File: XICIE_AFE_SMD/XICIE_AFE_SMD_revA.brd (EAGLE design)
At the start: 100 x 80 mm, 14 parts, among them IC1 LM324D, Q1 MOSFET-NCHANNELBSS123LT1G, Q2 MOSFET-NCHANNELBSS123LT1G

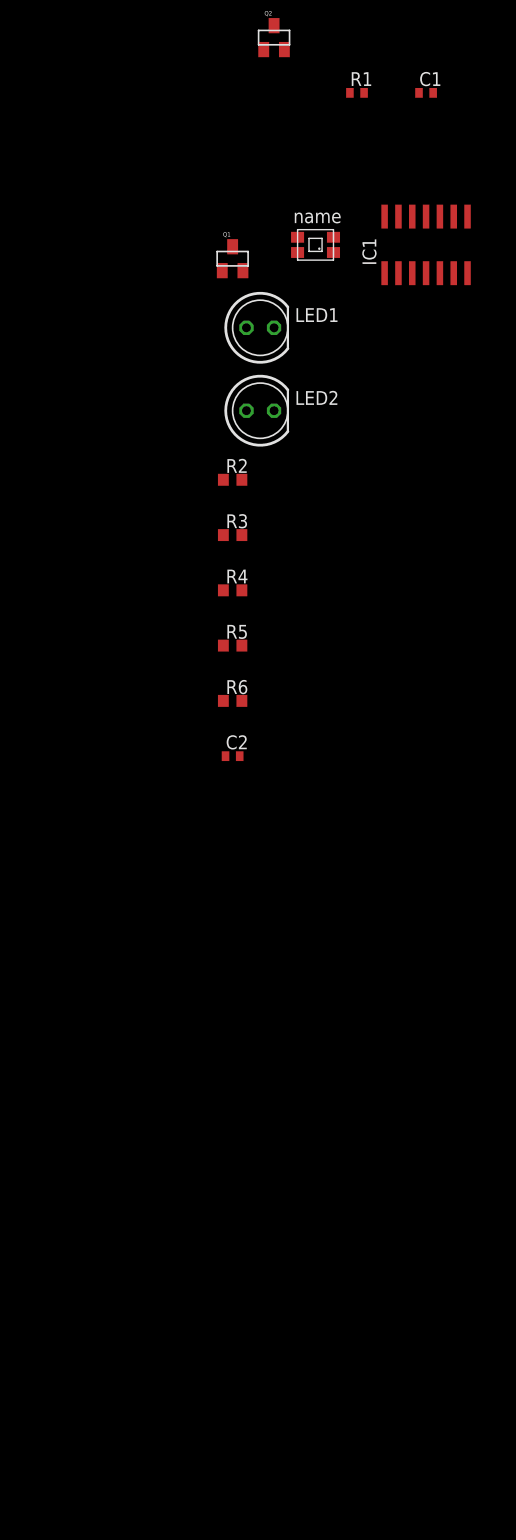
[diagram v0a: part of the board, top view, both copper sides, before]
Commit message: Added PSoc IC and boost converter
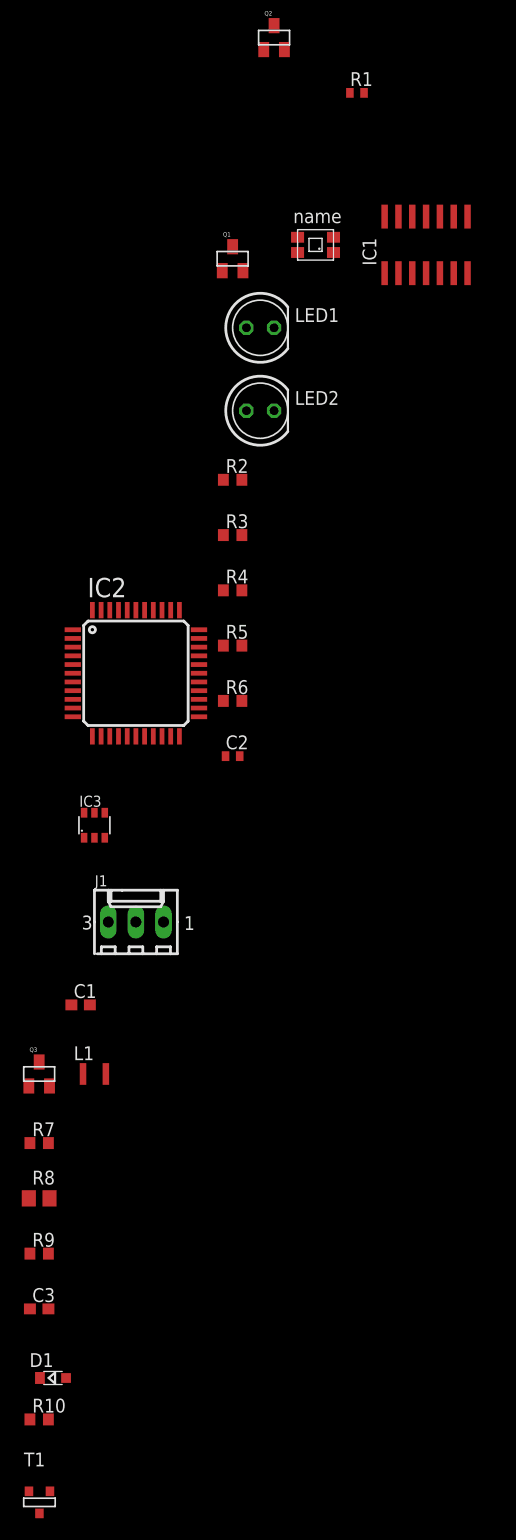
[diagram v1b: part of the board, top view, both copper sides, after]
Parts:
- added C3: 4.7 uF, rcl:C0603
- added D1: (no value), juliano:SMINI2-F5-B
- added IC2: CY8C4245T, juliano:TQFP44
- added IC3: AAT1217, juliano:SOT23-6
- added J1: 22-27-2031-03, con-molex:6410-03
- added L1: 4.7 uH, juliano:L2518
- added Q3: MOSFET-NCHANNELBSS123LT1G, SparkFun-DiscreteSemi:SOT23
- added R10, R7: 510 K, rcl:R0603
- added R8: 1.02 M, rcl:R0805
- added R9: 604 K, rcl:R0603
- added T1: (no value), zetex:SOT-23
- C1: value 270 pF -> 4.7 uF; device rcl:C0402 -> rcl:C0603
- moved C1 89.6 mm to (-50.8, -66.0)
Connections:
- removed net IN_VREF: R6.2
- removed net TRANSOUT: C1.2, IC1.1, R1.2
- new net N$10: C1.1, IC3.6, J1.3, L1.1
- new net N$11: D1.C, IC3.5, Q3.2, R7.2
- new net N$12: Q3.1, R7.1, T1.1
- new net N$13: IC3.4, R10.2
- new net N$14: IC3.3, R8.2, R9.1
- new net N$15: R10.1, T1.3
- new net N$2: D1.A, IC3.1, L1.2
- new net P0.6: IC2.30
- new net P1.2: IC2.39
- new net P2.2: IC2.4
- new net P2.6: IC2.8
- new net P3.6: IC2.17
- new net PWM_VREF: IC2.24, R6.2
- new net SENSOROUT: IC1.1, IC2.5, R1.2
- net GND: now also C1.2, C3.2, IC2.1, IC2.10, IC2.36, IC3.2, J1.2, R9.2, T1.2
- net IR: now also IC2.26
- net N$1: no longer C1.1
- net R: now also IC2.25
- net VCC: now also C3.1, IC2.35, Q3.3, R8.1
- net VREF: now also IC2.2

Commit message: PCB Layoutd
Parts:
- removed Q3: MOSFET-NCHANNELBSS123LT1G, SparkFun-DiscreteSemi:SOT23
- removed R10, R7: 510 K, rcl:R0603
- removed R5: 10, rcl:R0603
- removed T1: (no value), zetex:SOT-23
- R2, R3: value 10 -> 1.1; device rcl:R0603 -> rcl:R0402
- R4: value 10 -> 1.02 M; device rcl:R0603 -> rcl:R0805
- moved D1 184.7 mm to (36.1, 61.2), turned to 180 degrees
- moved C3 175.1 mm to (36.5, 55.5), turned to 180 degrees
- moved R9 169.4 mm to (32.1, 56.7), flipped to the bottom
- moved R8 166.2 mm to (36.4, 55.3), flipped to the bottom
- moved L1 160.7 mm to (36.4, 63.4), turned to 180 degrees
- moved C1 150.0 mm to (32.6, 58.6)
- moved J1 142.4 mm to (29.6, 62.4), turned to 180 degrees
- moved IC2 139.5 mm to (55.9, 60.0), flipped to the bottom
- moved IC3 138.3 mm to (36.7, 58.6), turned to 270 degrees
- moved C2 137.5 mm to (50.9, 62.7)
- moved R6 136.0 mm to (53.5, 63.6), turned to 90 degrees
- moved R4 115.7 mm to (39.8, 58.8), turned to 270 degrees
- moved R3 114.5 mm to (43.0, 59.1), turned to 180 degrees
- moved R2 112.8 mm to (43.0, 62.0), turned to 180 degrees
- moved LED2 104.8 mm to (45.0, 57.1)
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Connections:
- net N$2 renamed SW
- removed net N$10: C1.1, IC3.6, J1.3, L1.1
- removed net N$11: D1.C, IC3.5, Q3.2, R7.2
- removed net N$12: Q3.1, R7.1, T1.1
- removed net N$13: IC3.4, R10.2
- removed net N$15: R10.1, T1.3
- new net SHUTDOWN: IC3.4, R4.2
- new net VBAT: C1.1, IC3.6, J1.3, L1.1, R4.1
- net GND: no longer T1.2
- net N$7: no longer R5.1
- net N$8: no longer R4.1
- net VCC: now also D1.C, IC3.5; no longer Q3.3, R4.2, R5.2
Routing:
- net VCC: track 0.00 -> 37.3 mm, vias 0 -> 2
- net VREF: track 0.00 -> 24.2 mm, vias 0 -> 1
- net N$4: track 0.00 -> 14.3 mm, vias 0 -> 2
- net R: track 0.00 -> 13.5 mm, vias 0 -> 1
- net N$3: track 0.00 -> 11.5 mm
- net IR: track 0.00 -> 10.6 mm, vias 0 -> 1
- net VBAT: track 0.00 -> 8.83 mm
- net N$1: track 0.00 -> 8.25 mm
- net N$14: track 0.00 -> 6.16 mm, vias 0 -> 1
- net N$9: track 0.00 -> 5.68 mm
- net N$5: track 0.00 -> 2.75 mm
- net N$6: track 0.00 -> 2.45 mm
- net SENSOROUT: track 0.00 -> 2.42 mm
- net SHUTDOWN: track 0.00 -> 2.18 mm
- net N$8: track 0.00 -> 2.15 mm
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- added copper zone on layer 1, net GND
- added copper zone on layer 16, net GND
- added copper zone on layer 1, net SW
- added copper zone on layer 1, net VBAT
- added copper zone on layer 1, net VCC
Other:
- board size 100 x 80 mm -> 40.5 x 17.5 mm

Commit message: Finished layout
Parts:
- moved R6 5.42 mm to (50.8, 58.9), turned to 270 degrees
- moved Q2 3.45 mm to (48.2, 62.3)
- moved LED2 2.41 mm to (43.1, 55.7), turned to 270 degrees
- moved Q1 1.05 mm to (46.8, 54.5)
- moved R1 0.45 mm to (60.0, 62.5)
- moved U$1 0.38 mm to (56.7, 64.2)
- moved C2 0.35 mm to (50.9, 62.4), turned to 270 degrees
- moved IC1 0.30 mm to (56.7, 57.8)
- moved R3 0.25 mm to (42.8, 59.1)
- moved LED1 0.20 mm to (45.0, 63.9)
- moved R2 0.15 mm to (42.8, 62.0)
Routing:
- net VCC: track 37.3 -> 11.7 mm
- net R: track 13.5 -> 6.67 mm
- net VREF: track 24.2 -> 30.2 mm
- net PWM_VREF: track 0.00 -> 6.03 mm, vias 0 -> 1
- net SENSOROUT: track 2.42 -> 8.01 mm, vias 0 -> 1
- net VBAT: track 8.83 -> 3.40 mm
- net IR: track 10.6 -> 13.6 mm
- net N$14: track 6.16 -> 8.89 mm
- net GND: track 0.00 -> 2.59 mm, vias 0 -> 1
- net N$9: track 5.68 -> 8.22 mm
- net N$4: track 14.3 -> 15.1 mm, vias 2 -> 0
- net N$8: track 2.15 -> 2.88 mm
- net N$5: track 2.75 -> 2.16 mm
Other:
- board size 40.5 x 17.5 mm -> 42 x 18.5 mm

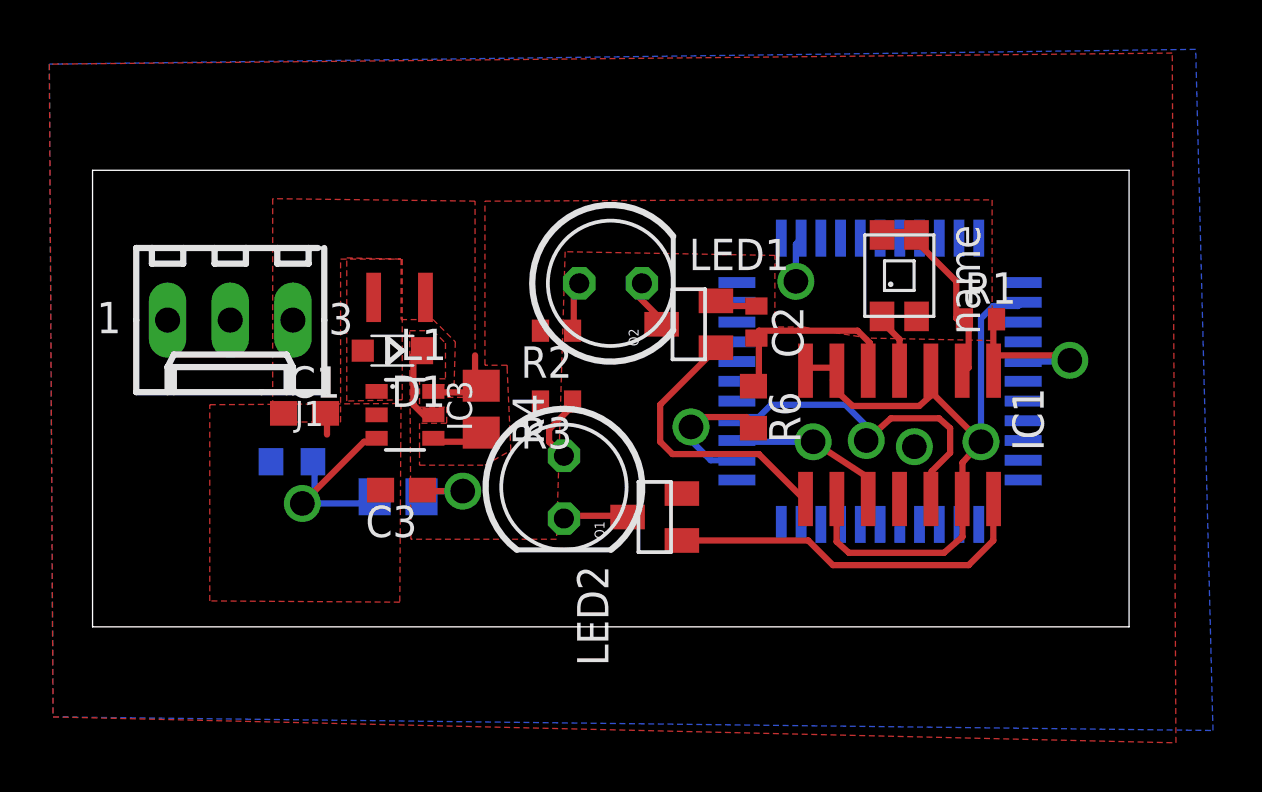
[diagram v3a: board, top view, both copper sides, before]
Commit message: Reduced outline
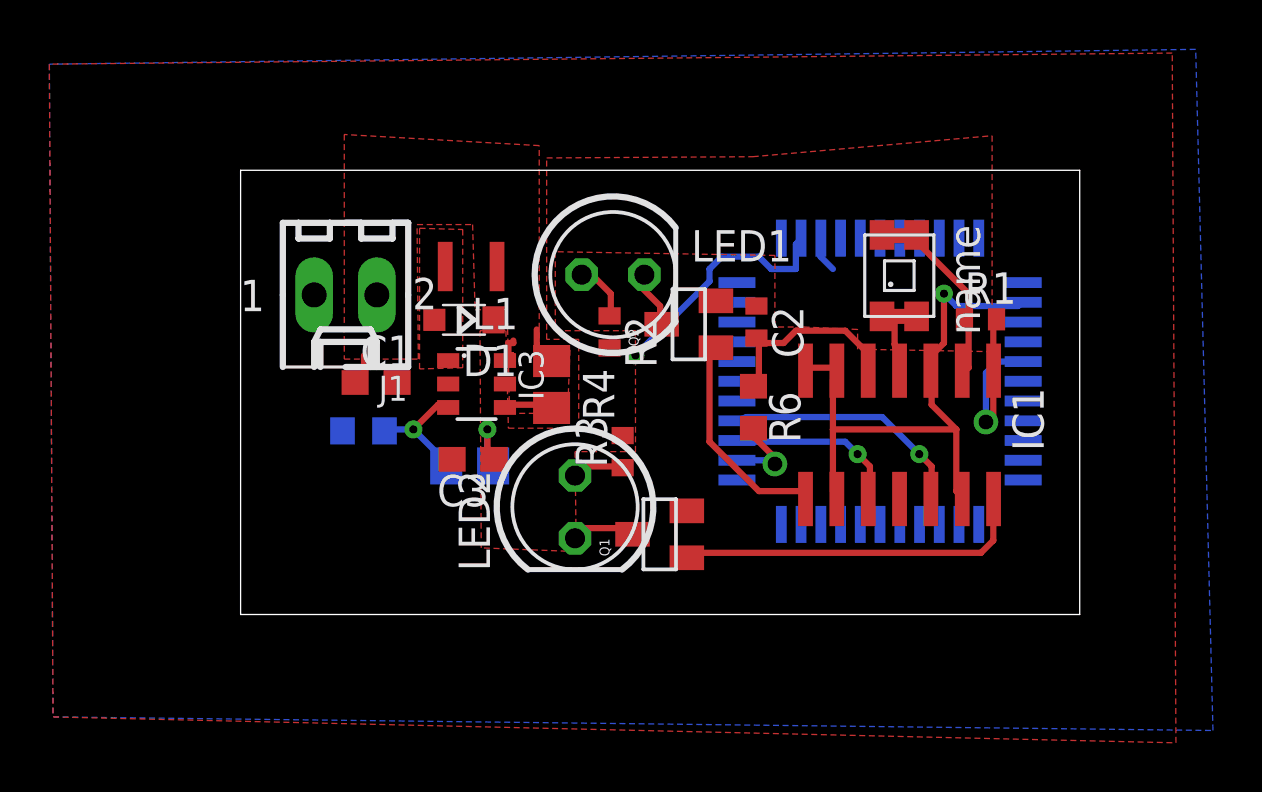
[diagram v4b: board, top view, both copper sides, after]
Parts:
- J1: value 22-27-2031-03 -> 22-27-2021-02; device con-molex:6410-03 -> con-molex:6410-02
- moved J1 4.78 mm to (34.2, 63.5)
- moved R3 3.36 mm to (45.5, 57.1), turned to 90 degrees
- moved IC3 3.16 mm to (39.6, 59.8)
- moved L1 3.16 mm to (39.3, 64.6)
- moved C1 3.16 mm to (35.5, 59.9)
- moved C3 3.16 mm to (39.4, 56.8)
- moved D1 3.16 mm to (39.0, 62.4)
- moved R8 3.16 mm to (39.3, 56.5)
- moved R9 3.16 mm to (35.0, 57.9)
- moved R4 3.02 mm to (42.6, 59.8)
- moved R2 2.15 mm to (45.0, 62.0), turned to 270 degrees
- moved LED2 0.92 mm to (43.5, 54.9)
- moved Q1 0.73 mm to (47.0, 53.8)
- moved LED1 0.36 mm to (45.1, 64.3)
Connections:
- net GND: now also J1.1; no longer J1.2
- net VBAT: now also J1.2; no longer J1.3
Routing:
- net VREF: track 30.2 -> 24.1 mm
- net VCC: track 11.7 -> 16.7 mm
- net N$14: track 8.89 -> 5.02 mm
- net IR: track 13.6 -> 10.1 mm
- net N$3: track 12.0 -> 9.07 mm
- net PWM_VREF: track 6.03 -> 3.73 mm
- net N$11: track 0.00 -> 1.40 mm
- net GND: track 2.59 -> 1.46 mm, vias 1 -> 0
- net N$10: track 0.00 -> 0.85 mm
- net N$7: track 2.02 -> 2.82 mm
- net N$4: track 15.1 -> 14.4 mm
- net N$8: track 2.88 -> 2.14 mm
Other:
- board size 42 x 18.5 mm -> 34 x 18 mm
